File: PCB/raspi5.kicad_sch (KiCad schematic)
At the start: 6 parts, among them J1 GPIO, J3 68711614522, U1 BL24C256A

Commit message: Version 1.2 routed
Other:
- title: Raspberry Pi 5 - GPIO & PCIe Headers -> Pi 5 - Artix XC7A50T - PCIe FPGA Hat
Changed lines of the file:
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@@
 	(paper "A4")
 	(title_block
-		(title "Raspberry Pi 5 - GPIO & PCIe Headers")
-		(date "2024-03-24")
-		(rev "1.1")
+		(title "Pi 5 - Artix XC7A50T - PCIe FPGA Hat")
+		(date "2025-07-17")
+		(rev "1.2")
 		(company "George Smart, M1GEO")
 		(comment 1 "https://github.com/m1geo/Pi5-Artix-FPGA-Hat")

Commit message: MIPI conectors should be now compatible with C597981
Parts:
- J3: footprint 68711614522 -> Wurth_68711614522:68711614522
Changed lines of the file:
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@@
 			)
 		)
-		(property "Footprint" "68711614522"
+		(property "Footprint" "Wurth_68711614522:68711614522"
 			(at 181.61 138.1 0)
 			(effects

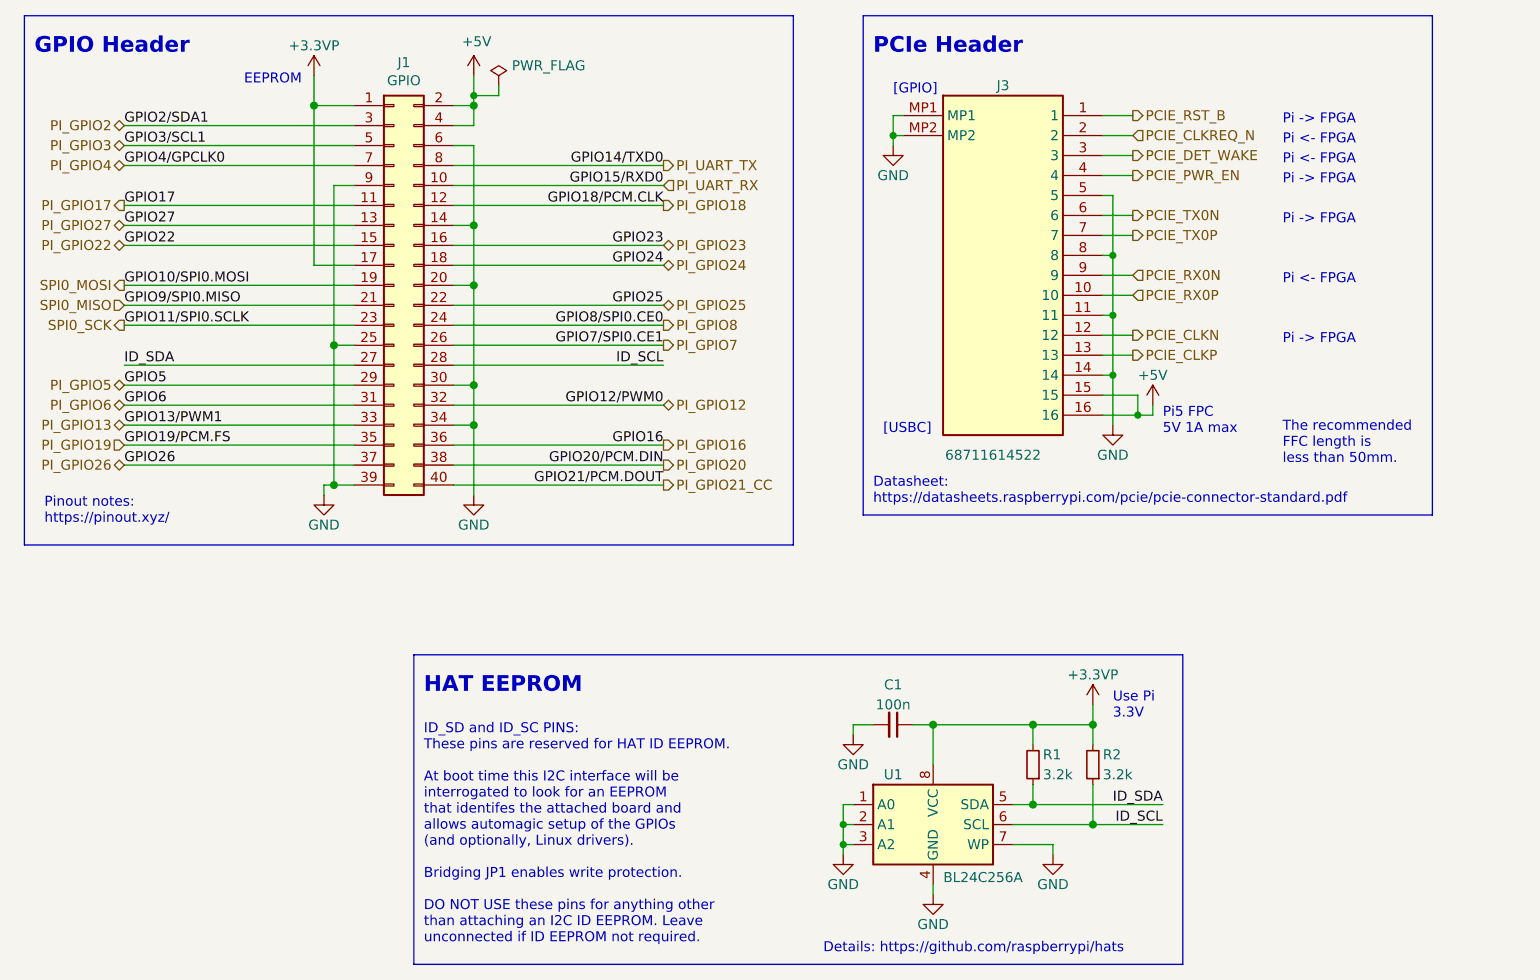
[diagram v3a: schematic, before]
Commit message: Updating LEDs footprint and Resistors value
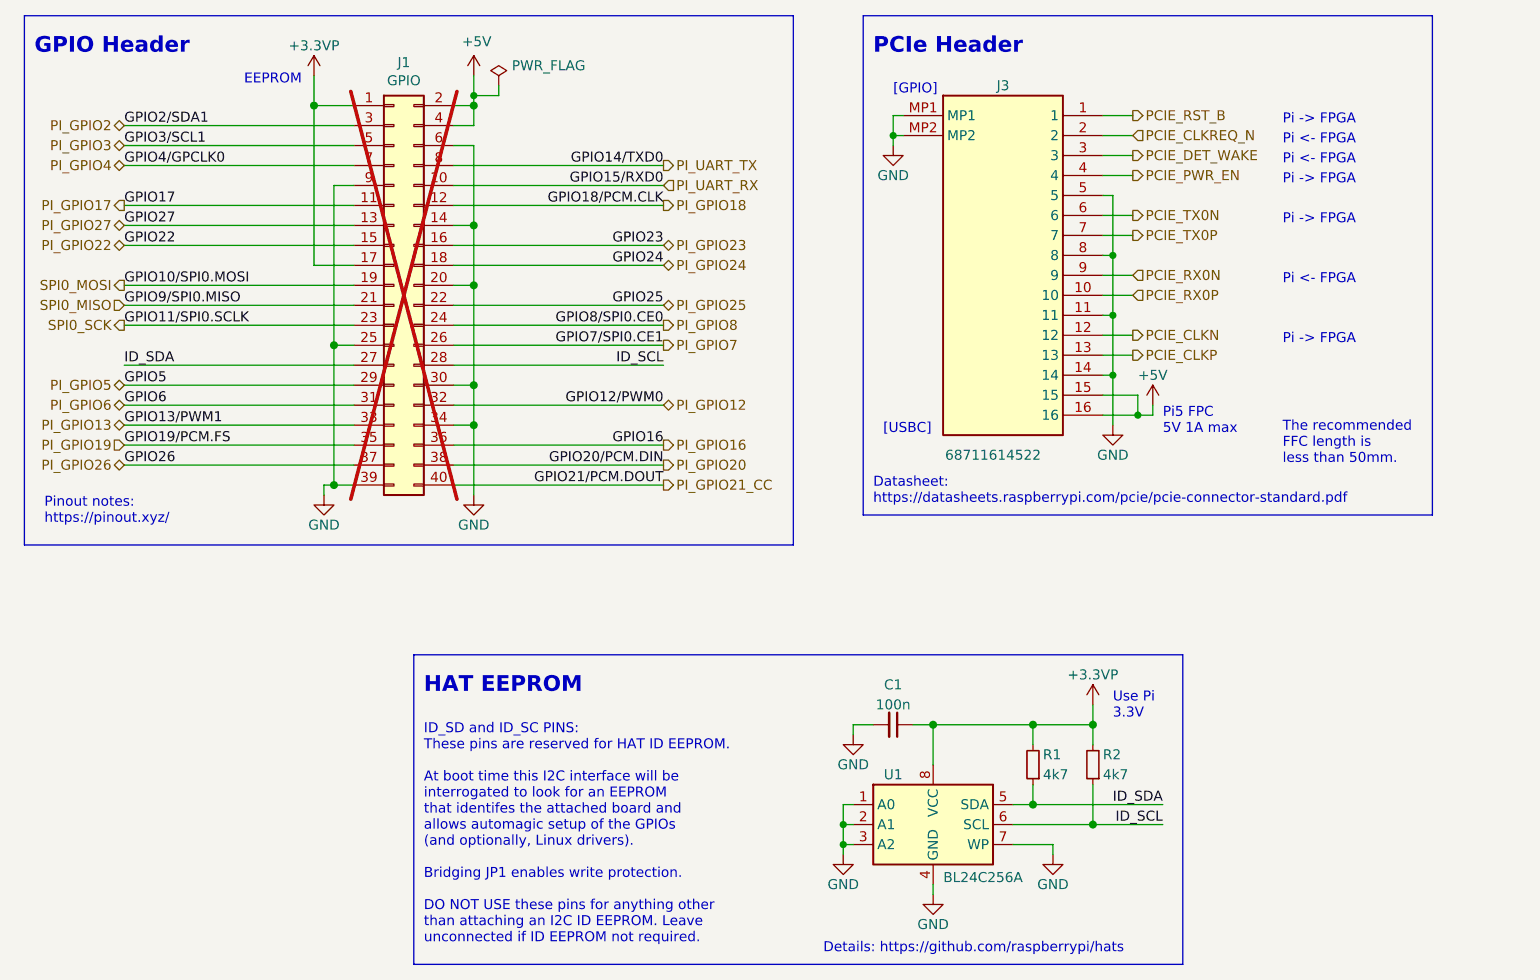
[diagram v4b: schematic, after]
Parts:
- J1: now not fitted; now left out of the parts list
- R1, R2: value 3.2k -> 4k7; LCSC C853935 -> C25900
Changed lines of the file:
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@@
 			)
 		)
-		(property "Value" "3.2k"
+		(property "Value" "4k7"
 			(at 185.42 127 0)
 			(effects
@@
 			)
 		)
-		(property "LCSC" "C853935"
+		(property "LCSC" "C25900"
 			(at 184.15 125.73 0)
 			(effects
@@
 		(unit 1)
 		(exclude_from_sim no)
-		(in_bom yes)
-		(on_board yes)
-		(dnp no)
+		(in_bom no)
+		(on_board yes)
+		(dnp yes)
 		(property "Reference" "J1"
 			(at 96.52 36.4298 0)
@@
 			)
 		)
-		(property "Value" "3.2k"
+		(property "Value" "4k7"
 			(at 177.8 127 0)
 			(effects
@@
 			)
 		)
-		(property "LCSC" "C853935"
+		(property "LCSC" "C25900"
 			(at 176.53 125.73 0)
 			(effects
